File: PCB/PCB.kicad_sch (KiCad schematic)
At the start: 84 parts, among them J1 USB_B_Micro, Q1 PJA3428, Q2 PJA3428, Q3 AO3401A, SW1 SW_Push, SW2 SW_Push, SW3 SW_Push, SW4 ON/OFF, U1 ESP32-PICO-MINI-02, U2 CP2102N-Axx-xQFN24, U3 TP4056, U4 TPS63051RMWR, U5 BNO080, Y1 32.768 kHz, Y2 32.768 kHz

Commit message: buck-boost delete
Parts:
- removed C12: 10uF, symbol Device:C_Small
- removed C13: 1.3nF, symbol Device:C_Small
- removed L1: 1.5uH, symbol Device:L
- removed U4: TPS63051RMWR, QFN50P250X250X100-12N, symbol TPS63051RMWR:TPS63051RMWR

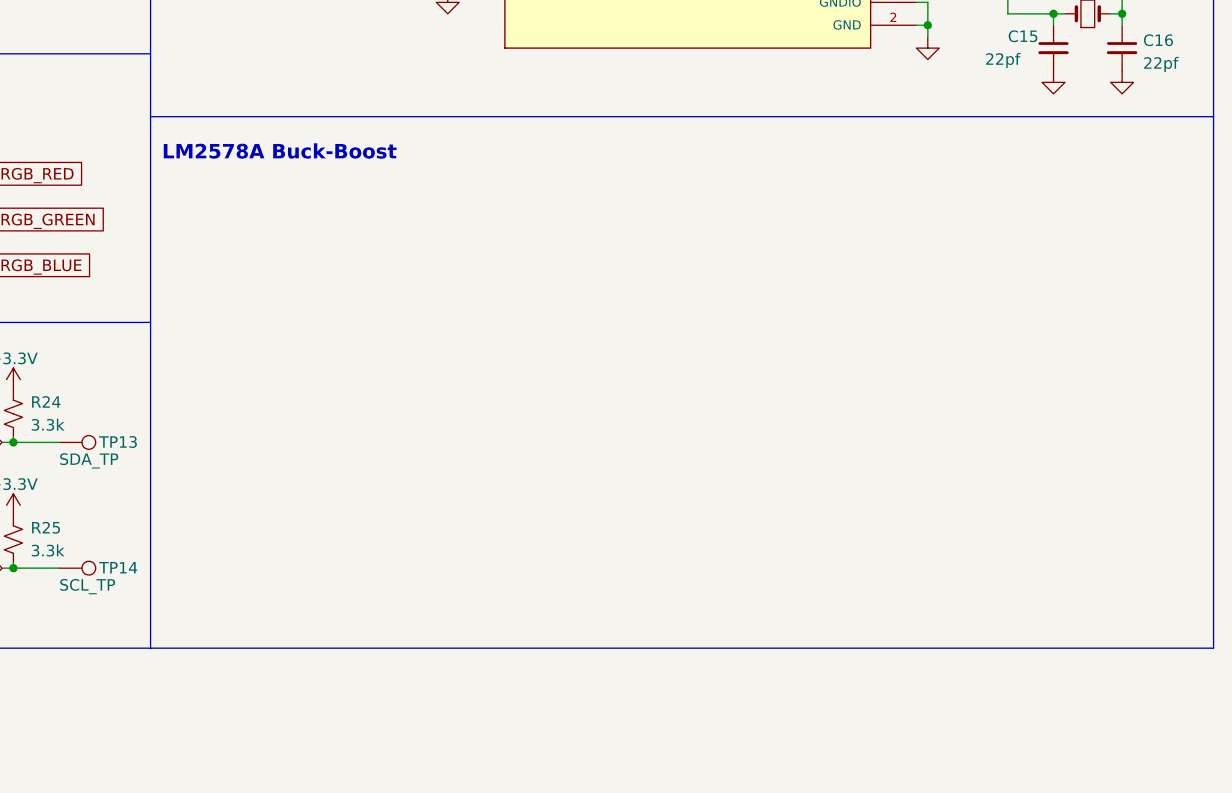
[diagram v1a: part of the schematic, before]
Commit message: buck-boost pcb
buck-boost added to pcb
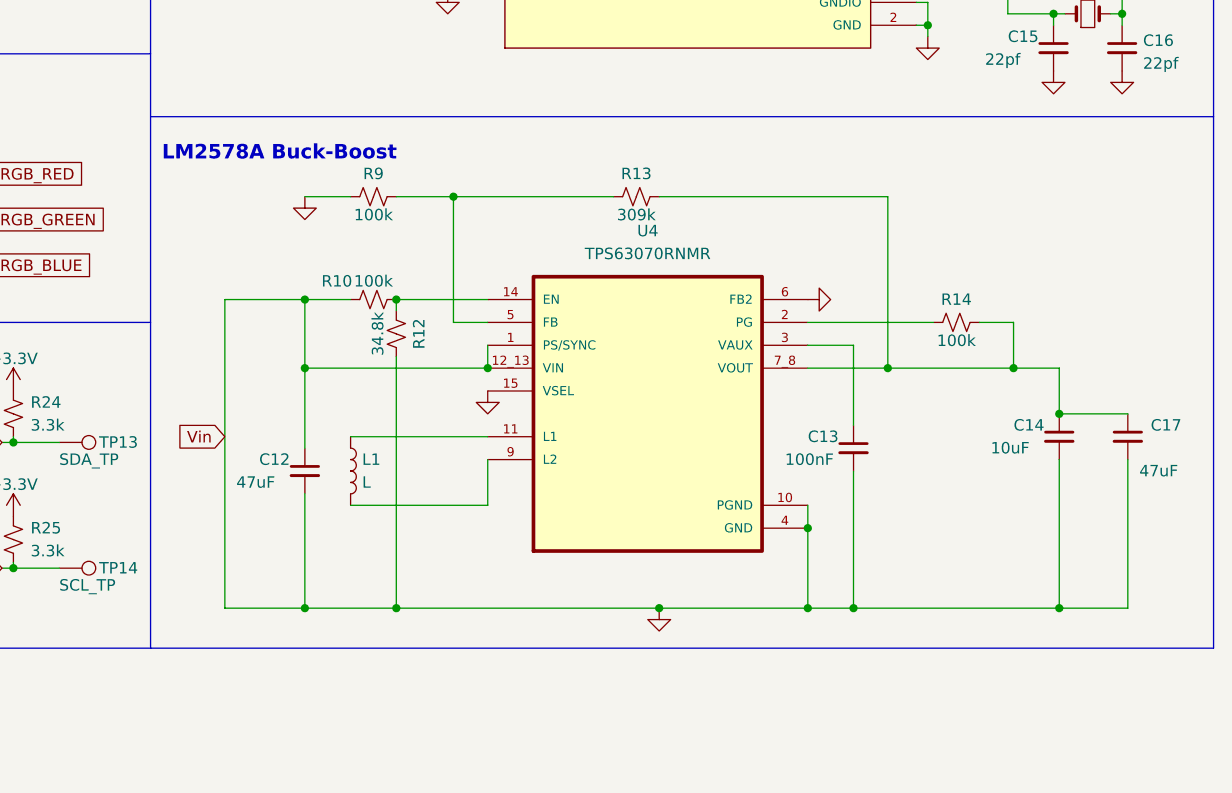
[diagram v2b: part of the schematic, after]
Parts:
- added C12, C17: 47uF, Capacitor_SMD:C_0603_1608Metric, symbol Device:C_Small
- added C13: 100nF, Capacitor_SMD:C_0603_1608Metric, symbol Device:C_Small
- added C14: 10uF, Capacitor_SMD:C_0603_1608Metric, symbol Device:C_Small
- added L1: L, symbol Device:L
- added R10, R14, R9: 100k, Resistor_SMD:R_0603_1608Metric, symbol Device:R_Small_US
- added R12: 34.8k, Resistor_SMD:R_0603_1608Metric, symbol Device:R_Small_US
- added R13: 309k, Resistor_SMD:R_0603_1608Metric, symbol Device:R_Small_US
- added U4: TPS63070RNMR, VREG_TPS63070RNMR, symbol TPS63070RNMR:TPS63070RNMR
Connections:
- net Vin is gone; now on net GND: C7.2, F1.2, R19.1, TP3.1
- net GND: now also C12.1, C12.2, C13.2, C14.2, C17.2, R10.1, R12.1, R9.2, U4.1 (PS/SYNC), U4.10 (PGND), U4.12_13 (VIN), U4.15 (VSEL), U4.4 (GND), U4.6 (FB2)
- new net: R10.2, R12.2, U4.14 (EN)
- new net: C13.1, U4.3 (VAUX)
- new net: C14.1, C17.1, R13.1, R14.1, U4.7_8 (VOUT)
- new net: R13.2, R9.1, U4.5 (FB)
- new net: L1.1, U4.11 (L1)
- new net: R14.2, U4.2 (PG)
- new net: L1.2, U4.9 (L2)

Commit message: bb_check
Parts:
- U4: footprint VREG_TPS63070RNMR -> TPS63070RNMR:VREG_TPS63070RNMR
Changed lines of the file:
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@@
     (property "Reference" "U4" (id 0) (at 344.17 101.6 0))
     (property "Value" "TPS63070RNMR" (id 1) (at 344.17 104.14 0))
-    (property "Footprint" "VREG_TPS63070RNMR" (id 2) (at 344.17 121.92 0)
+    (property "Footprint" "TPS63070RNMR:VREG_TPS63070RNMR" (id 2) (at 344.17 121.92 0)
       (effects (font (size 1.27 1.27)) (justify left bottom) hide)
     )
@@
     )
     (path "/54b1a856-06a2-4795-8f0d-fe5a8e16418b"
-      (reference "U4") (unit 1) (value "TPS63070RNMR") (footprint "VREG_TPS63070RNMR")
+      (reference "U4") (unit 1) (value "TPS63070RNMR") (footprint "TPS63070RNMR:VREG_TPS63070RNMR")
     )
     (path "/eacacdb2-ba7e-471f-9bac-6f3c29d249db"

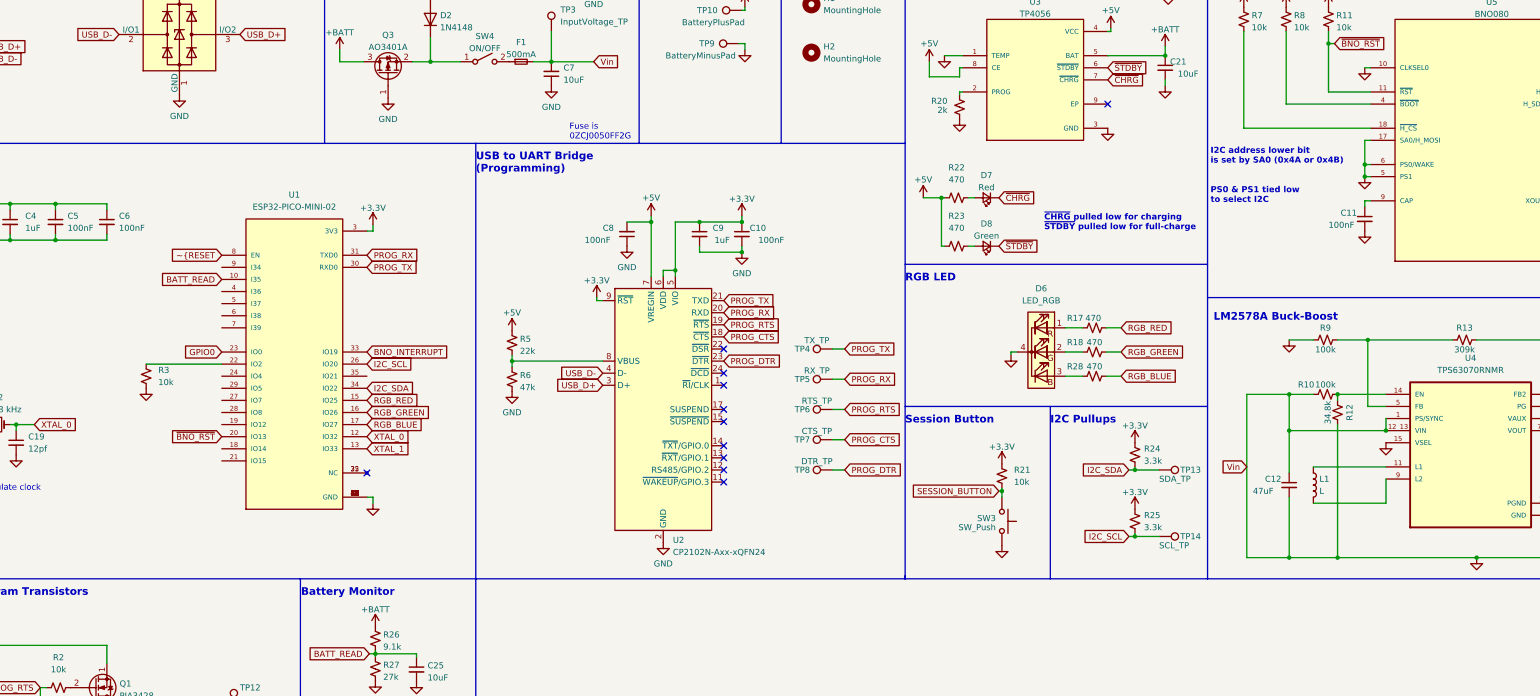
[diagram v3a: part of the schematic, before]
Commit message: updates based on in lab feedback and errors
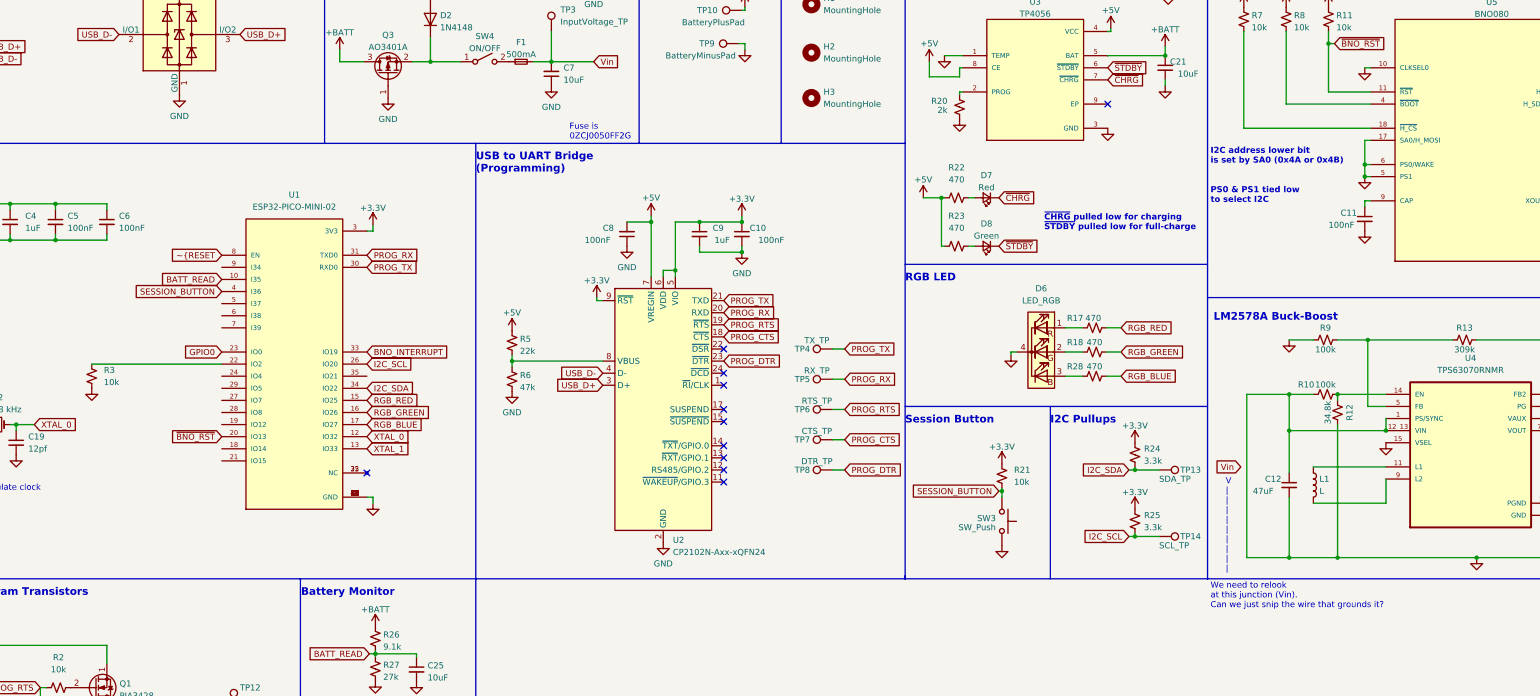
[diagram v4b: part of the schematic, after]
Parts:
- added H3: MountingHole, MountingHole:MountingHole_2.2mm_M2_Pad_Via, symbol Mechanical:MountingHole
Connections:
- net GND: no longer C7.2, F1.2, R19.1, TP3.1
- net SESSION_BUTTON: now also U1.4 (I36)
- new net Vin: C7.2, F1.2, R19.1, TP3.1
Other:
- note added: "V | | | | | | | | |"
- note added: "We need to relook at this junction (Vin). Can we just snip the wire that grounds it?"
- moved on the sheet: R3
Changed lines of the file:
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@@
     (stroke (width 0) (type default) (color 0 0 0 0))
   )
-  (wire (pts (xy 66.04 102.87) (xy 81.915 102.87))
+  (wire (pts (xy 54.61 102.87) (xy 81.915 102.87))
     (stroke (width 0) (type default) (color 0 0 0 0))
   )
@@
     (effects (font (size 1.6 1.6) (thickness 0.32) bold) (justify left bottom))
   )
+  (text "We need to relook \nat this junction (Vin).\nCan we just snip the wire that grounds it?"
+    (at 289.56 154.305 0)
+    (effects (font (size 1.27 1.27)) (justify left bottom))
+  )
   (text "ESP32\n" (at 13.335 60.325 0)
     (effects (font (size 1.6 1.6) (thickness 0.32) bold) (justify left bottom))
@@
     (effects (font (size 1.27 1.27) bold) (justify left bottom))
   )
+  (text "V\n|\n|\n|\n|\n|\n|\n|\n|\n|" (at 292.735 146.685 0)
+    (effects (font (size 1.27 1.27)) (justify left bottom))
+  )
   (text "ESP32 Auto-Program Transistors" (at 13.335 151.765 0)
     (effects (font (size 1.6 1.6) (thickness 0.32) bold) (justify left bottom))
@@
     )
   )
+  (global_label "SESSION_BUTTON" (shape input) (at 81.915 87.63 180) (fields_autoplaced)
+    (effects (font (size 1.27 1.27)) (justify right))
+    (property "Intersheet References" "${INTERSHEET_REFS}" (id 0) (at 63.2943 87.5506 0)
+      (effects (font (size 1.27 1.27)) (justify right) hide)
+    )
+  )
   (global_label "PROG_DTR" (shape input) (at 31.115 161.925 180) (fields_autoplaced)
     (effects (font (size 1.27 1.27)) (justify right))
@@
     )
   )
-  (global_label "Vin" (shape input) (at 297.18 124.46 180) (fields_autoplaced)
+  (global_label "Vin" (shape input) (at 295.91 124.46 180) (fields_autoplaced)
     (effects (font (size 1.27 1.27)) (justify right))
-    (property "Intersheet References" "${INTERSHEET_REFS}" (id 0) (at 291.9245 124.3806 0)
+    (property "Intersheet References" "${INTERSHEET_REFS}" (id 0) (at 290.6545 124.3806 0)
       (effects (font (size 1.27 1.27)) (justify right) hide)
     )
@@
     (pin "2")
   )
-  (symbol (lib_id "Device:R_Small_US") (at 66.04 105.41 180) (unit 1)
+  (symbol (lib_id "Device:R_Small_US") (at 54.61 105.41 180) (unit 1)
     (in_bom yes) (on_board yes) (fields_autoplaced)
-    (property "Reference" "R3" (id 0) (at 68.58 104.1399 0)
+    (property "Reference" "R3" (id 0) (at 57.15 104.1399 0)
       (effects (font (size 1.27 1.27)) (justify right))
     )
-    (property "Value" "10k" (id 1) (at 68.58 106.6799 0)
+    (property "Value" "10k" (id 1) (at 57.15 106.6799 0)
       (effects (font (size 1.27 1.27)) (justify right))
     )
-    (property "Footprint" "Resistor_SMD:R_0603_1608Metric" (id 2) (at 66.04 105.41 0)
+    (property "Footprint" "Resistor_SMD:R_0603_1608Metric" (id 2) (at 54.61 105.41 0)
       (effects (font (size 1.27 1.27)) hide)
     )
-    (property "Datasheet" "~" (id 3) (at 66.04 105.41 0)
+    (property "Datasheet" "~" (id 3) (at 54.61 105.41 0)
       (effects (font (size 1.27 1.27)) hide)
     )
@@
     (pin "2")
   )
-  (symbol (lib_id "power:GND") (at 66.04 107.95 0) (unit 1)
+  (symbol (lib_id "power:GND") (at 54.61 107.95 0) (unit 1)
     (in_bom yes) (on_board yes) (fields_autoplaced)
-    (property "Reference" "#PWR0107" (id 0) (at 66.04 114.3 0)
+    (property "Reference" "#PWR0107" (id 0) (at 54.61 114.3 0)
       (effects (font (size 1.27 1.27)) hide)
     )
-    (property "Value" "GND" (id 1) (at 66.04 112.3934 0)
+    (property "Value" "GND" (id 1) (at 54.61 112.3934 0)
       (effects (font (size 1.27 1.27)) hide)
     )
-    (property "Footprint" "" (id 2) (at 66.04 107.95 0)
+    (property "Footprint" "" (id 2) (at 54.61 107.95 0)
       (effects (font (size 1.27 1.27)) hide)
     )
-    (property "Datasheet" "" (id 3) (at 66.04 107.95 0)
+    (property "Datasheet" "" (id 3) (at 54.61 107.95 0)
       (effects (font (size 1.27 1.27)) hide)
     )
@@
     (pin "1")
   )
+  (symbol (lib_id "Mechanical:MountingHole") (at 205.74 46.99 0) (unit 1)
+    (in_bom yes) (on_board yes) (fields_autoplaced)
+    (property "Reference" "H3" (id 0) (at 208.28 45.7199 0)
+      (effects (font (size 1.27 1.27)) (justify left))
+    )
+    (property "Value" "MountingHole" (id 1) (at 208.28 48.2599 0)
+      (effects (font (size 1.27 1.27)) (justify left))
+    )
+    (property "Footprint" "MountingHole:MountingHole_2.2mm_M2_Pad_Via" (id 2) (at 205.74 46.99 0)
+      (effects (font (size 1.27 1.27)) hide)
+    )
+    (property "Datasheet" "~" (id 3) (at 205.74 46.99 0)
+      (effects (font (size 1.27 1.27)) hide)
+    )
+  )
   (symbol (lib_id "BNO080:BNO080") (at 348.615 55.88 0) (unit 1)
     (in_bom yes) (on_board yes) (fields_autoplaced)
@@
       (reference "H2") (unit 1) (value "MountingHole") (footprint "MountingHole:MountingHole_2.2mm_M2_Pad_Via")
     )
+    (path "/e89aac88-ce90-478a-89fc-a8199972cbde"
+      (reference "H3") (unit 1) (value "MountingHole") (footprint "MountingHole:MountingHole_2.2mm_M2_Pad_Via")
+    )
     (path "/e63a89f5-7297-4989-a102-d835e84994e7"

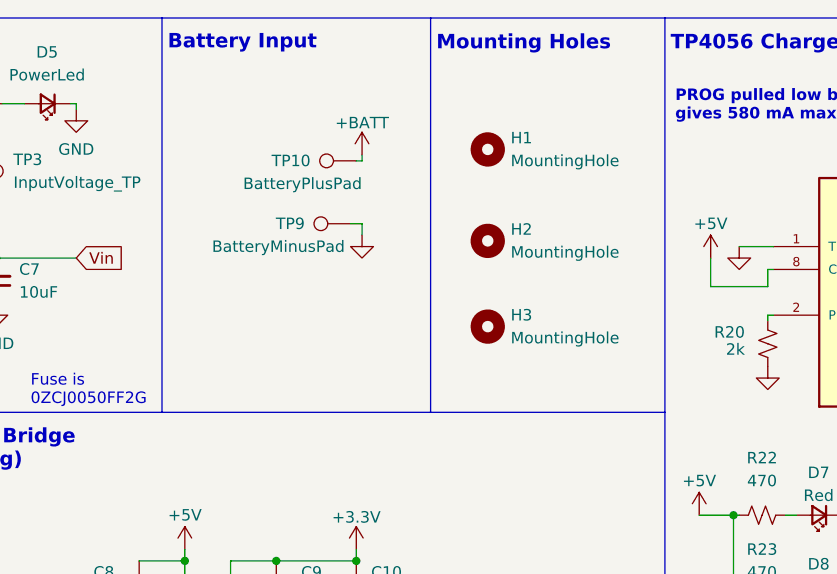
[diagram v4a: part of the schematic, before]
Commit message: update power connector and silkscreen
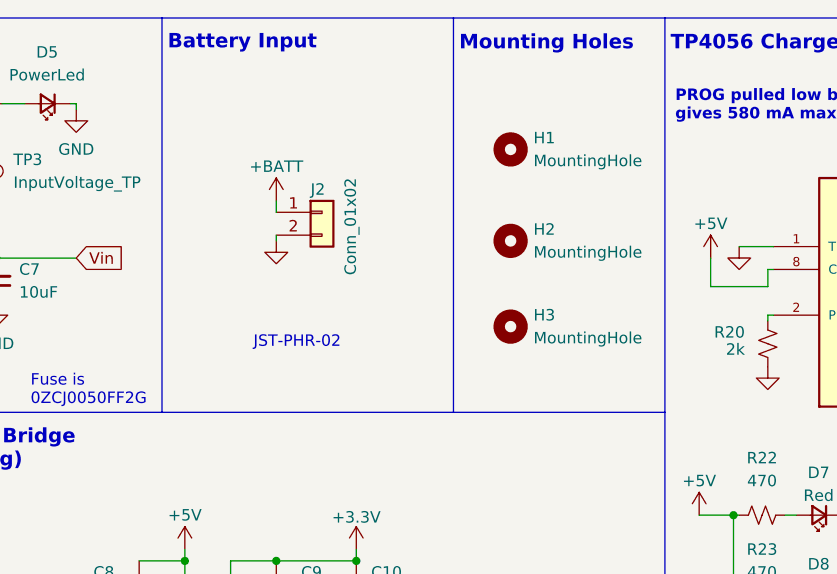
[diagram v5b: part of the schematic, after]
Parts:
- removed TP10: BatteryPlusPad, TestPoint:TestPoint_THTPad_D2.5mm_Drill1.2mm, symbol Connector:TestPoint
- removed TP9: BatteryMinusPad, TestPoint:TestPoint_THTPad_D2.5mm_Drill1.2mm, symbol Connector:TestPoint
- added J2: Conn_01x02, PHR-2:JST_PHR-2, symbol Connector_Generic:Conn_01x02
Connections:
- net +BATT: now also J2.1 (Pin_1)
- net GND: now also J2.2 (Pin_2)
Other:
- note added: "JST-PHR-02"
- moved on the sheet: H1, H2, H3
